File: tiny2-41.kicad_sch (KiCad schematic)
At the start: 21 parts, among them J1 Conn_01x01_Male, J10 Conn_01x01_Male, J11 Conn_01x01_Male, J12 Conn_01x01_Male, J2 Conn_01x01_Male, J20 Conn_01x04_Female, J21 Conn_01x08_Male, J3 Conn_01x01_Male, J4 Conn_01x01_Male, J5 Conn_01x01_Male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

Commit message: Updated
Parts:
- added U?: MB85RS1MT, symbol Memory_NVRAM:MB85RS1MT
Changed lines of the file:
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@@
+    (pin "8")
+  )
+  (symbol (lib_id "Memory_NVRAM:MB85RS1MT") (at 120.65 156.21 0) (unit 1)
+    (in_bom yes) (on_board yes) (fields_autoplaced)
+    (property "Reference" "U?" (id 0) (at 122.6694 146.05 0)
+      (effects (font (size 1.27 1.27)) (justify left))
+    )
+    (property "Value" "MB85RS1MT" (id 1) (at 122.6694 148.59 0)
+      (effects (font (size 1.27 1.27)) (justify left))
+    )
+    (property "Footprint" "" (id 2) (at 111.76 157.48 0)
+      (effects (font (size 1.27 1.27)) hide)
+    )
+    (property "Datasheet" "http://www.fujitsu.com/downloads/MICRO/fsa/pdf/products/memory/fram/MB85RS16-DS501-00014-6v0-E.pdf" (id 3) (at 111.76 157.48 0)
+      (effects (font (size 1.27 1.27)) hide)
+    )
+    (pin "1")
+    (pin "2")
+    (pin "3")
+    (pin "4")
+    (pin "5")
+    (pin "6")
+    (pin "7")
     (pin "8")
   )
@@
       (reference "U3") (unit 1) (value "Pico") (footprint "MCU_RaspberryPi_and_Boards:RPi_Pico_LiPo_SMD_TH")
     )
-  )
+    (path "/be00b103-0ee7-47ac-8b76-205c8812ee09"
+      (reference "U?") (unit 1) (value "MB85RS1MT") (footprint "")
+    )
+  )

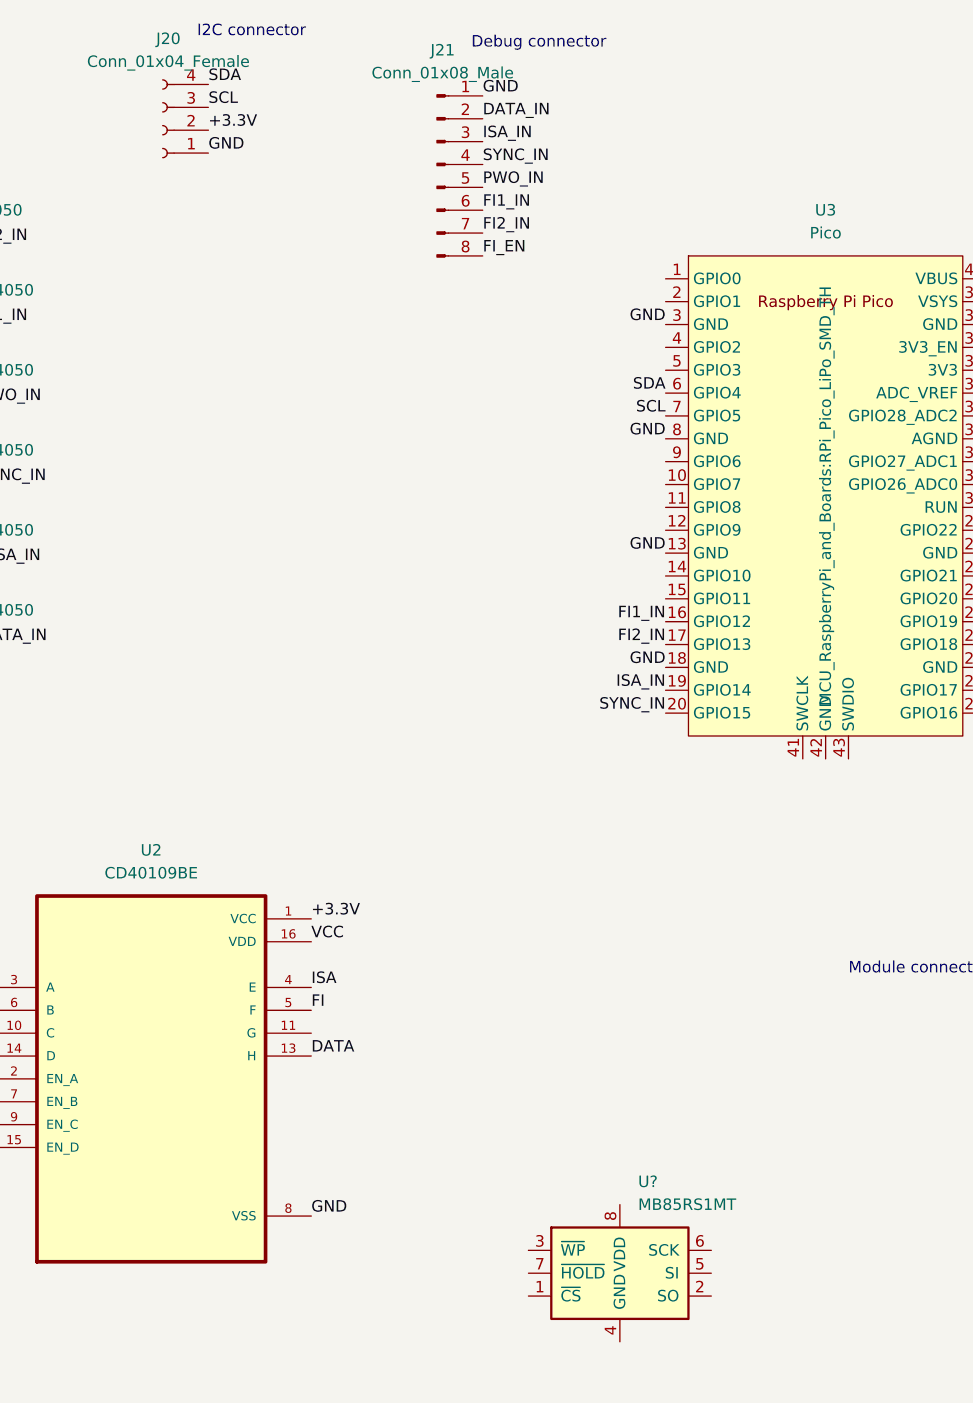
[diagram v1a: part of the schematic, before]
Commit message: Added FRAM
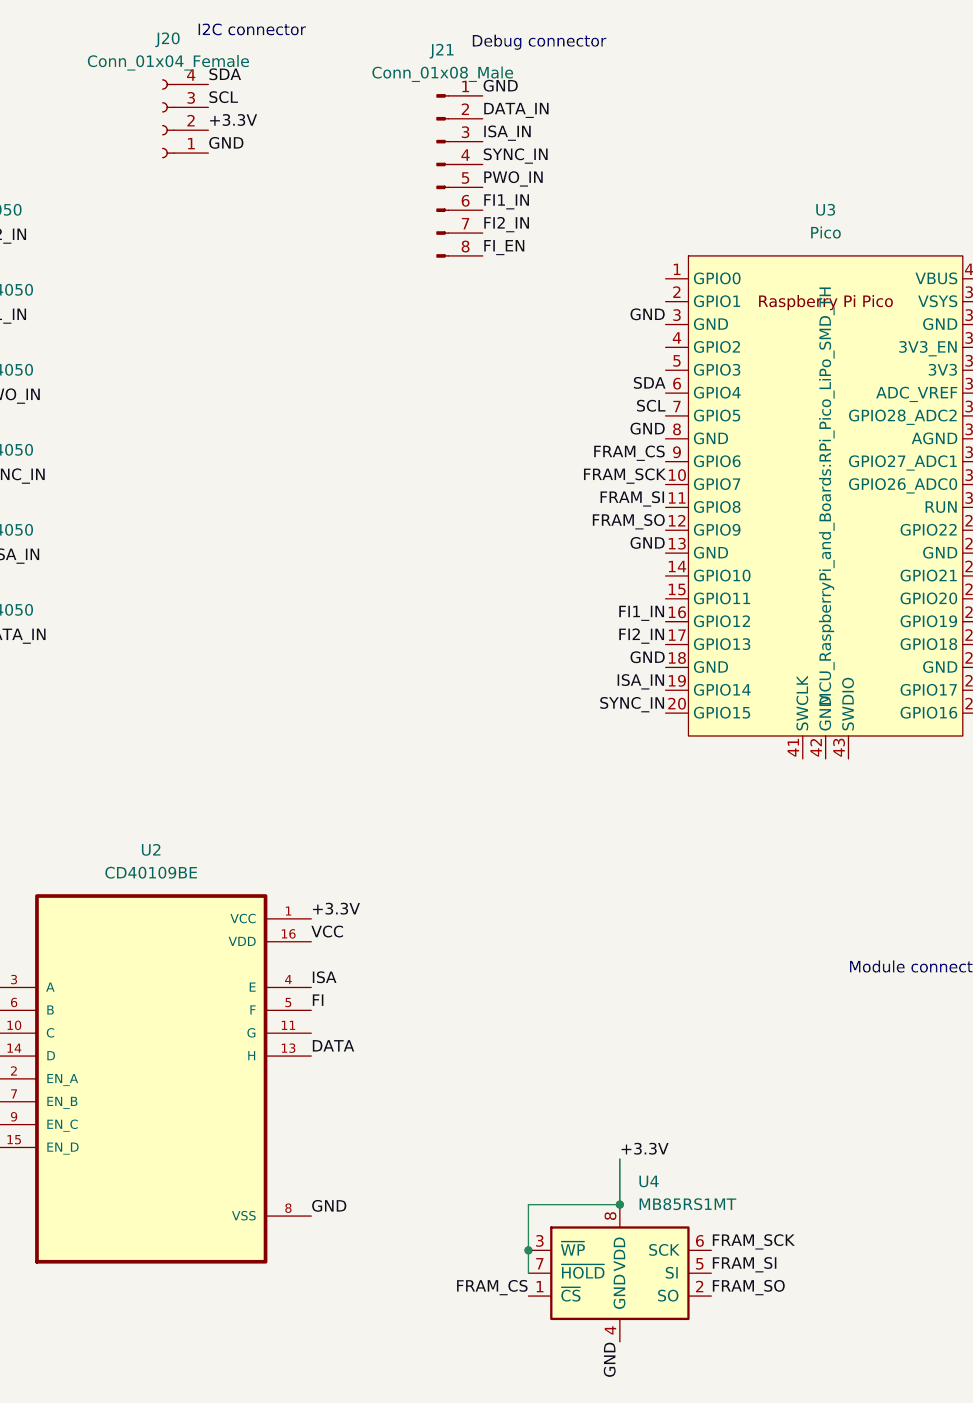
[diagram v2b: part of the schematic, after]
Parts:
- gave numbers to parts that had none: 1
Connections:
- net +3.3V: now also U4.3 (~{WP}), U4.7 (~{HOLD}), U4.8 (VDD)
- net GND: now also U4.4 (GND)
- net FRAM_CS: now reaches U4.1 (~{CS})
- net FRAM_CS: now also U3.9 (GPIO6)
- net FRAM_SO: now reaches U4.2 (SO)
- net FRAM_SO: now also U3.12 (GPIO9)
- net FRAM_SI: now reaches U4.5 (SI)
- net FRAM_SI: now also U3.11 (GPIO8)
- net FRAM_SCK: now reaches U4.6 (SCK)
- net FRAM_SCK: now also U3.10 (GPIO7)

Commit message: Updated ...
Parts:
- removed U4: MB85RS1MT, symbol Memory_NVRAM:MB85RS1MT
- added IC1: MB85RC1MTPNF-G-JNERE1, KiCad:SOIC127P600X175-8N, symbol MB85RC1MTPNF-G-JNERE1:MB85RC1MTPNF-G-JNERE1
- added RN1: R_Network06, KiCad:4607X101105LF, symbol Device:R_Network06
- R2, R3: value 100k -> R
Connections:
- net +3.3V: now also R2.1, R3.1, IC1.8 (VDD)
- net DATA: now also RN1.3 (R2); no longer R2.1
- net FI1: now also RN1.7 (R6)
- net FI2: now also RN1.6 (R5)
- net GND: now also IC1.2 (A1), IC1.3 (A2), IC1.4 (VSS), RN1.1 (common); no longer R2.2, R3.2
- net ISA: now also RN1.4 (R3); no longer R3.1
- net PWO: now also RN1.2 (R1)
- net SCL: now also R3.2, IC1.6 (SCL)
- net SDA: now also R2.2, IC1.5 (SDA)
- net SYNC: now also RN1.5 (R4)
- net FRAM_CS renamed FRAM_EN
- net FRAM_EN: now also IC1.7 (WP)
- net FRAM_SCK: no longer names the net of U3.10 (GPIO7)
- net FRAM_SI: no longer names the net of U3.11 (GPIO8)
- net FRAM_SO: no longer names the net of U3.12 (GPIO9)
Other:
- note added: "I2C Pullups"
- note added: "IR Output"
- moved on the sheet: J1, J10, J11, J12, J2, J20, J21, J3, J4, J5, J6, J7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
